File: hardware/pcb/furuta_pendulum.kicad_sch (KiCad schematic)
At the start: 72 parts, among them J2 LCD_ST7735S, J3 DRV8313, J4 SWD, J7 Encoders, J8 USB_C_Receptacle_USB2.0_14P, SW1 TS-1088-AR02016, SW2 TS-1088-AR02016, U1 AMS1117-3.3, U3 USBLC6-2SC6, U7 ATSAMD51J20A-A

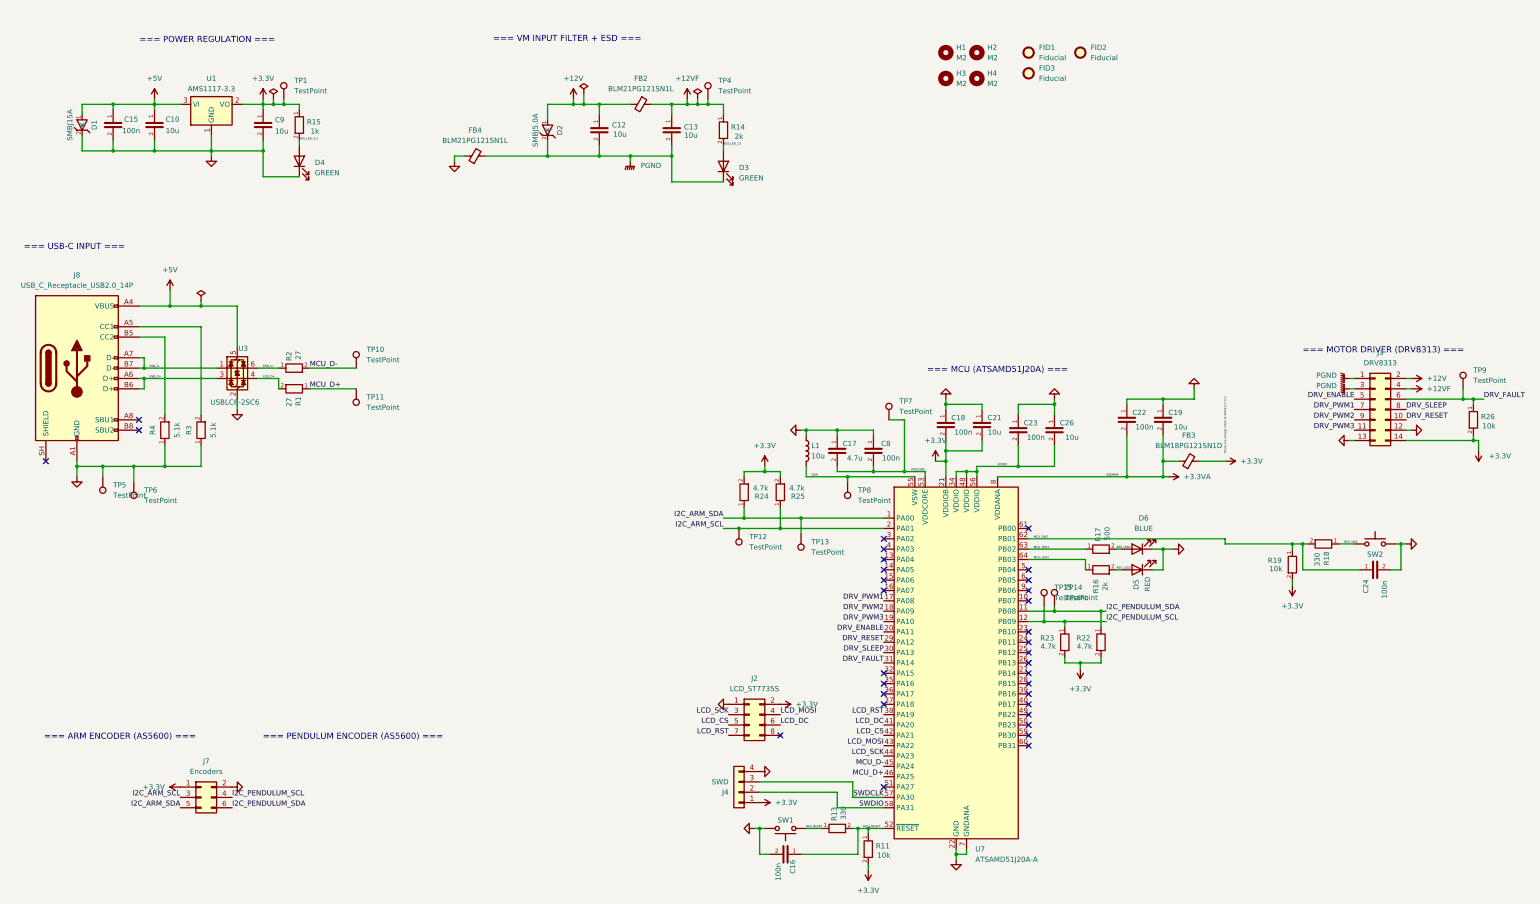
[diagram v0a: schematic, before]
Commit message: Update PCB docs: TVS diodes, pi-filter, Tag-Connect SWD, SWO
Co-authored-by: Copilot <223556219+Copilot@users.noreply.github.com>
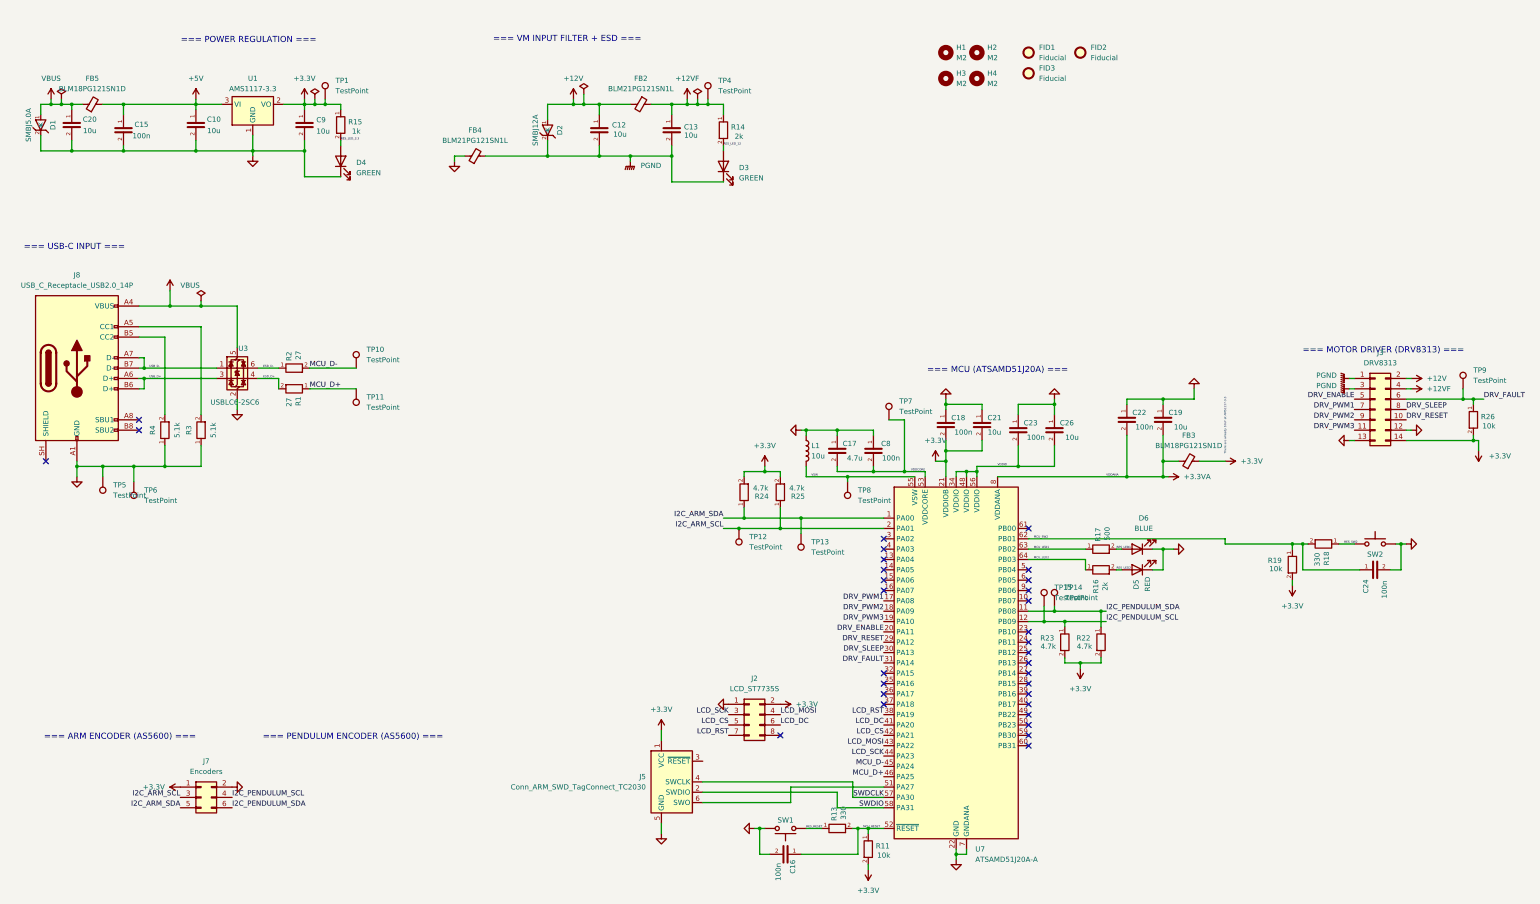
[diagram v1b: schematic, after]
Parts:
- removed J4: SWD, Connector_PinHeader_1.27mm:PinHeader_1x04_P1.27mm_Vertical, symbol Connector_Generic:Conn_01x04
- added C20: 10u, Capacitor_SMD:C_0805_2012Metric, symbol Device:C
- added FB5: BLM18PG121SN1D, Inductor_SMD:L_0402_1005Metric, symbol Device:FerriteBead_Small
- added J5: Conn_ARM_SWD_TagConnect_TC2030, Connector:Tag-Connect_TC2030-IDC-FP_2x03_P1.27mm_Vertical, symbol Connector:Conn_ARM_SWD_TagConnect_TC2030
- D1: value SMBJ15A -> SMBJ5.0A
- D2: value SMBJ5.0A -> SMBJ12A
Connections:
- net +3.3V: now also J5.1 (VCC)
- net +5V: now also FB5.2; no longer D1.1 (A), J8.A4 (VBUS), J8.A9 (VBUS), J8.B4 (VBUS), J8.B9 (VBUS), U3.5 (VBUS)
- net GND: now also C20.2, J5.5 (GND)
- net SWDCLK: now also J5.4 (SWCLK)
- net SWDIO: now also J5.2 (SWDIO)
- net at U7.51 (PA27): now also J5.6 (SWO)
- new net VBUS: C20.1, D1.1 (A), FB5.1, J8.A4 (VBUS), J8.A9 (VBUS), J8.B4 (VBUS), J8.B9 (VBUS), U3.5 (VBUS)
- no-connect marks 32 -> 31
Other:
- moved on the sheet: C10, C9, D1, D4, R15, TP1, U1

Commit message: PCB Rev 1 — production release to JLCPCB
Includes final schematic and layout changes, production files (Gerbers,
BOM, positions), JLCPCB component mapping, Claude Code project instructions
and MCP config, and component datasheet.

Co-Authored-By: Claude Sonnet 4.6 <noreply@anthropic.com>
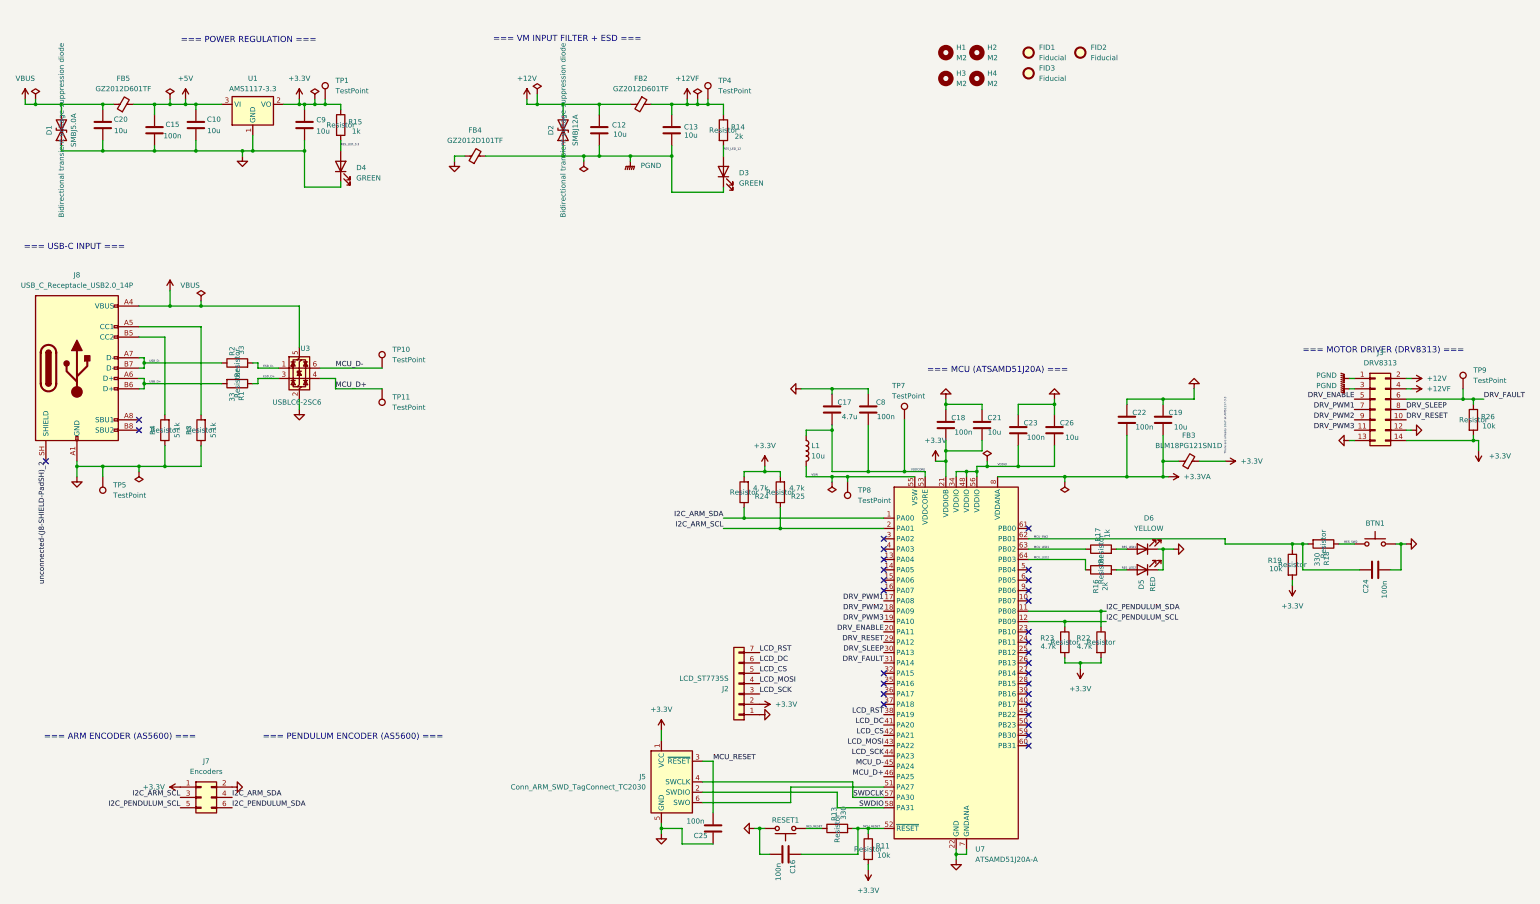
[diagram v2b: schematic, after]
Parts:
- removed TP12, TP13, TP14, TP15, TP6: TestPoint, TestPoint:TestPoint_Pad_D1.5mm, symbol Connector:TestPoint
- added C25: 100n, Capacitor_SMD:C_0402_1005Metric, symbol Device:C
- BTN1: renamed from SW2; LCSC Part # (none) -> C720477
- C10, C12, C13, C19, C20, C26, C9: LCSC Part # (none) -> C440198
- C15, C16, C18, C22, C23, C24, C8: LCSC Part # (none) -> C1525
- C17: LCSC Part # (none) -> C19666
- C21: footprint Capacitor_SMD:C_0603_1608Metric -> Capacitor_SMD:C_0805_2012Metric; LCSC Part # (none) -> C440198
- D3, D4: footprint LED_SMD:LED_0402_1005Metric -> LED_SMD:LED_0805_2012Metric; LCSC Part # (none) -> C2297
- D5: footprint LED_SMD:LED_0402_1005Metric -> LED_SMD:LED_0603_1608Metric; LCSC Part # (none) -> KT-0603R
- D6: value BLUE -> YELLOW; footprint LED_SMD:LED_0402_1005Metric -> LED_SMD:LED_0805_2012Metric; KiLib_Generator (none) -> 1=K 2=A; LCSC Part # (none) -> KT-0805Y
- FB2: value BLM21PG121SN1L -> GZ2012D601TF; LCSC Part # (none) -> C1017
- FB3: footprint Inductor_SMD:L_0402_1005Metric -> Inductor_SMD:L_0603_1608Metric; LCSC Part # (none) -> C14709
- FB4: value BLM21PG121SN1L -> GZ2012D101TF; LCSC Part # (none) -> C1015
- FB5: value BLM18PG121SN1D -> GZ2012D601TF; footprint Inductor_SMD:L_0402_1005Metric -> Inductor_SMD:L_0805_2012Metric; LCSC Part # (none) -> C1017
- J2: footprint Connector_PinHeader_2.54mm:PinHeader_2x04_P2.54mm_Vertical -> Connector_PinHeader_2.54mm:PinHeader_1x07_P2.54mm_Vertical; symbol Connector_Generic:Conn_02x04_Odd_Even -> Connector_Generic:Conn_01x07
- J7: footprint Connector_PinHeader_2.54mm:PinHeader_2x03_P2.54mm_Vertical -> Connector_PinHeader_2.54mm:PinHeader_1x06_P2.54mm_Vertical
- L1: LCSC Part # (none) -> C1035
- R1, R2: value 27 -> 33; LCSC Part # (none) -> C25105
- R11, R19, R26: LCSC Part # (none) -> C25744
- R13, R18: LCSC Part # (none) -> C25104
- R14, R16: LCSC Part # (none) -> C4109
- R15: LCSC Part # (none) -> C11702
- R17: value 500 -> 1k; LCSC Part # (none) -> C11702
- R22, R23, R24, R25: LCSC Part # (none) -> C25900
- R3, R4: LCSC Part # (none) -> C25905
- RESET1: renamed from SW1; LCSC Part # (none) -> C720477
- U1: LCSC Part # (none) -> C6186
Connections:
- net +12V: now also D2.2 (A2); no longer D2.1 (A)
- net ESD_D+: now also R1.1, U3.3 (I/O2); no longer R1.2, U3.4 (I/O2)
- net ESD_D-: now also R2.2, U3.1 (I/O1); no longer R2.1, U3.6 (I/O1)
- net GND: now also D1.1 (A1), C25.1; no longer D1.2 (K), L1.1
- net I2C_ARM_SDA: now also J7.4 (Pin_4); no longer J7.5 (Pin_5)
- net I2C_PENDULUM_SCL: now also J7.5 (Pin_5); no longer J7.4 (Pin_4)
- net MCU_D+: now also U3.4 (I/O2); no longer R1.1
- net MCU_D-: now also U3.6 (I/O1); no longer R2.2
- net MCU_RESET: now also J5.3 (~{RESET}), C25.2
- net PGND: now also D2.1 (A1); no longer D2.2 (K)
- net USB_D+: now also R1.2; no longer U3.3 (I/O2)
- net USB_D-: now also R2.1; no longer U3.1 (I/O1)
- net VBUS: now also D1.2 (A2); no longer D1.1 (A)
- net VDDCORE: now also L1.1
- net unconnected-(J8-SHIELD-PadSH)_2: now reaches J8.SH (SHIELD)
- no-connect marks 31 -> 30
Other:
- moved on the sheet: D3, D4, D5, D6, FB5, TP10, TP11, TP7, U3
